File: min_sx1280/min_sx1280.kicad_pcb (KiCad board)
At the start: 2 copper layers, 19.8 x 16.8 mm, 15 parts, among them J1 Conn_01x04, SW1 SW_SPST, U1 ME6211C33, U2 ESP-01F, U3 LoRa1280

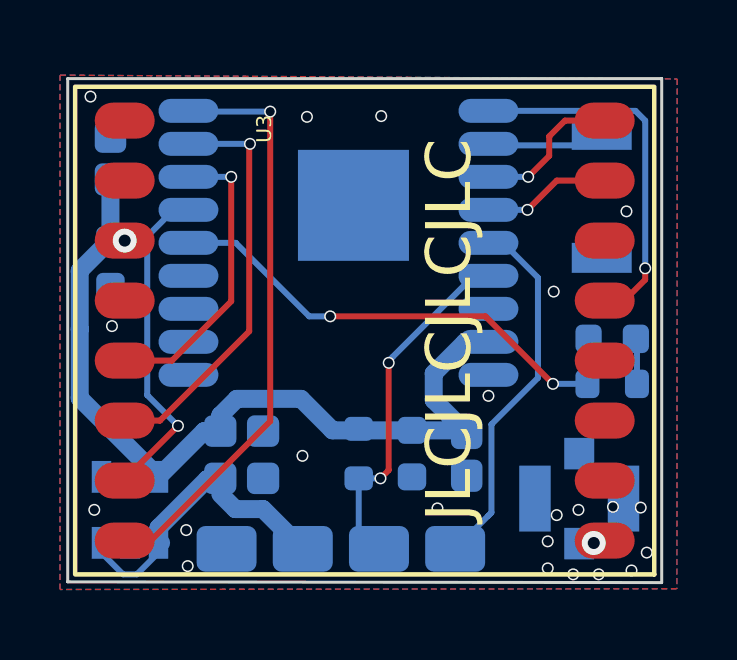
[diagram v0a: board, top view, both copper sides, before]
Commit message: Added anti-ripping vias, generated new gerbers and added some documentation.
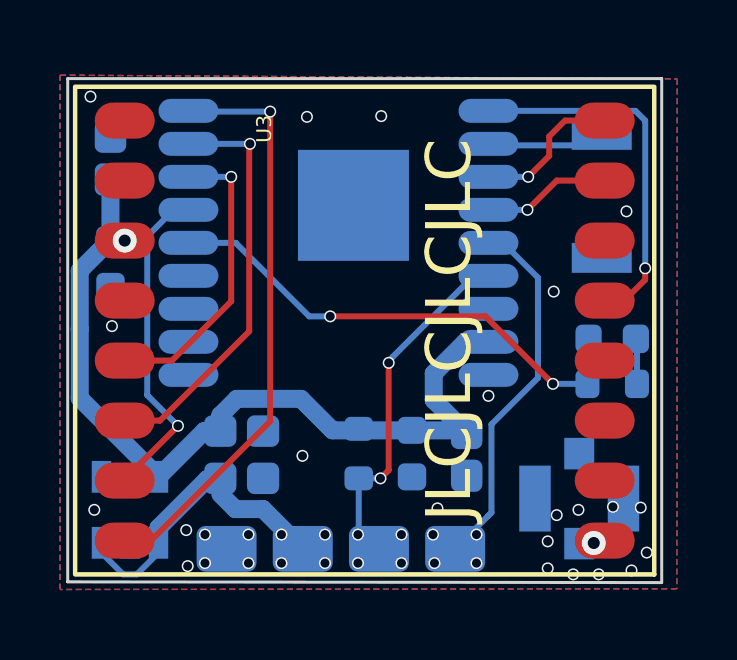
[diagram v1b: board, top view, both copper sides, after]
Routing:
- net +5V: track 9.99 -> 9.91 mm, vias 0 -> 4
- net GND: vias 22 -> 26
- net /TX: vias 2 -> 6
- net /RX: vias 0 -> 4
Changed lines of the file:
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@@
     (style (thickness 0.15) (arrow_length 1.27) (text_position_mode 0) (extension_height 0.58642) (extension_offset 0.5) keep_text_aligned)
   )
+  (via (at 105.85 143.9) (size 0.4) (drill 0.3) (layers "F.Cu" "B.Cu") (net 1))
   (via (at 103.775 142.8) (size 0.4) (drill 0.3) (layers "F.Cu" "B.Cu") (net 1))
   (via (at 116.85 142.125) (size 0.4) (drill 0.3) (layers "F.Cu" "B.Cu") (net 1))
@@
   (via (at 118.45 132.175) (size 0.4) (drill 0.3) (layers "F.Cu" "B.Cu") (net 1))
   (via (at 107.65 140.325) (size 0.4) (drill 0.3) (layers "F.Cu" "B.Cu") (net 1))
+  (via (at 104.4 143.9) (size 0.4) (drill 0.3) (layers "F.Cu" "B.Cu") (net 1))
   (via (at 116.675 144.275) (size 0.4) (drill 0.3) (layers "F.Cu" "B.Cu") (net 1))
   (via (at 100.584 128.35) (size 0.4) (drill 0.3) (layers "F.Cu" "B.Cu") (net 1))
   (via (at 113.85 138.325) (size 0.4) (drill 0.3) (layers "F.Cu" "B.Cu") (net 1))
   (via (at 116.125 142.3) (size 0.4) (drill 0.3) (layers "F.Cu" "B.Cu") (net 1))
+  (via (at 104.4 142.95) (size 0.4) (drill 0.3) (layers "F.Cu" "B.Cu") (net 1))
   (via (at 118.925 142.05) (size 0.4) (drill 0.3) (layers "F.Cu" "B.Cu") (net 1))
   (via (at 101.3 136) (size 0.4) (drill 0.3) (layers "F.Cu" "B.Cu") (net 1))
@@
   (via (at 117.525 144.275) (size 0.4) (drill 0.3) (layers "F.Cu" "B.Cu") (net 1))
   (via (at 116.025 134.85) (size 0.4) (drill 0.3) (layers "F.Cu" "B.Cu") (net 1))
+  (via (at 105.85 142.95) (size 0.4) (drill 0.3) (layers "F.Cu" "B.Cu") (net 1))
   (via (at 115.825 144.075) (size 0.4) (drill 0.3) (layers "F.Cu" "B.Cu") (net 1))
   (via (at 112.15 142.075) (size 0.4) (drill 0.3) (layers "F.Cu" "B.Cu") (net 1))
@@
   (segment (start 116.895057 143.229943) (end 116.875 143.25) (width 0.4) (layer "B.Cu") (net 2))
   (segment (start 117.360625 143.229943) (end 116.895057 143.229943) (width 0.4) (layer "B.Cu") (net 2))
+  (via (at 108.4 143.9) (size 0.4) (drill 0.3) (layers "F.Cu" "B.Cu") (net 3))
+  (via (at 108.4 142.95) (size 0.4) (drill 0.3) (layers "F.Cu" "B.Cu") (net 3))
+  (via (at 106.95 143.9) (size 0.4) (drill 0.3) (layers "F.Cu" "B.Cu") (net 3))
+  (via (at 106.95 142.95) (size 0.4) (drill 0.3) (layers "F.Cu" "B.Cu") (net 3))
   (segment (start 102.85 142.725) (end 102.85 143.225) (width 0.6) (layer "B.Cu") (net 3))
   (segment (start 102.85 143.225) (end 102.85 143.55428) (width 0.2) (layer "B.Cu") (net 3))
   (segment (start 106.33501 142.10001) (end 105.41251 142.10001) (width 0.6) (layer "B.Cu") (net 3))
-  (segment (start 102.85 143.225) (end 102.9375 143.225) (width 0.6) (layer "B.Cu") (net 3))
   (segment (start 102.85 143.55428) (end 102.12928 144.275) (width 0.2) (layer "B.Cu") (net 3))
   (segment (start 100.95 143.55428) (end 100.95 143.225) (width 0.2) (layer "B.Cu") (net 3))
@@
   (segment (start 110.525 137.225) (end 110.525 140.8) (width 0.2) (layer "F.Cu") (net 6))
   (segment (start 110.525 140.8) (end 110.25 141.075) (width 0.2) (layer "F.Cu") (net 6))
+  (via (at 109.5 143.9) (size 0.4) (drill 0.3) (layers "F.Cu" "B.Cu") (net 6))
   (via (at 110.525 137.225) (size 0.4) (drill 0.3) (layers "F.Cu" "B.Cu") (net 6))
+  (via (at 110.95 142.95) (size 0.4) (drill 0.3) (layers "F.Cu" "B.Cu") (net 6))
+  (via (at 110.95 143.9) (size 0.4) (drill 0.3) (layers "F.Cu" "B.Cu") (net 6))
+  (via (at 109.5 142.95) (size 0.4) (drill 0.3) (layers "F.Cu" "B.Cu") (net 6))
   (via (at 110.25 141.075) (size 0.4) (drill 0.3) (layers "F.Cu" "B.Cu") (net 6))
   (segment (start 109.525 141.075) (end 109.525 142.75) (width 0.2) (layer "B.Cu") (net 6))
@@
   (segment (start 110.660037 137.025) (end 110.525 137.160037) (width 0.2) (layer "B.Cu") (net 6))
   (segment (start 110.25 141.075) (end 109.525 141.075) (width 0.2) (layer "B.Cu") (net 6))
+  (via (at 112.05 143.9) (size 0.4) (drill 0.3) (layers "F.Cu" "B.Cu") (net 7))
+  (via (at 112 142.95) (size 0.4) (drill 0.3) (layers "F.Cu" "B.Cu") (net 7))
+  (via (at 113.45 142.95) (size 0.4) (drill 0.3) (layers "F.Cu" "B.Cu") (net 7))
+  (via (at 113.45 143.9) (size 0.4) (drill 0.3) (layers "F.Cu" "B.Cu") (net 7))
   (segment (start 113.95001 142.21499) (end 113.95001 139.27499) (width 0.2) (layer "B.Cu") (net 7))
   (segment (start 114.339963 133.225) (end 113.85 133.225) (width 0.2) (layer "B.Cu") (net 7))
